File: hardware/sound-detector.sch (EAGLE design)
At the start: 36 parts, among them U1 LMV324

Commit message: Updating 3k3 resistor to Sparkle part.
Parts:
- R12: device SparkFun-Resistors:RESISTOR0603-RES -> SparkFun-Resistors:3.3KOHM1/10W1%(0603)
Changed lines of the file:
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@@
 <part name="GND7" library="SparkFun-Aesthetics" deviceset="GND" device=""/>
 <part name="R11" library="SparkFun-Resistors" deviceset="100KOHM1/10W1%(0603)" device="" value="100k"/>
-<part name="R12" library="SparkFun-Resistors" deviceset="RESISTOR" device="0603-RES" value="3k3"/>
+<part name="R12" library="SparkFun-Resistors" deviceset="3.3KOHM1/10W1%(0603)" device="" value="3k3"/>
 <part name="R13" library="SparkFun-Resistors" deviceset="1KOHM1/10W1%(0603)" device="" value="1K"/>
 <part name="R14" library="SparkFun-Resistors" deviceset="100KOHM1/10W1%(0603)" device="" value="100k"/>

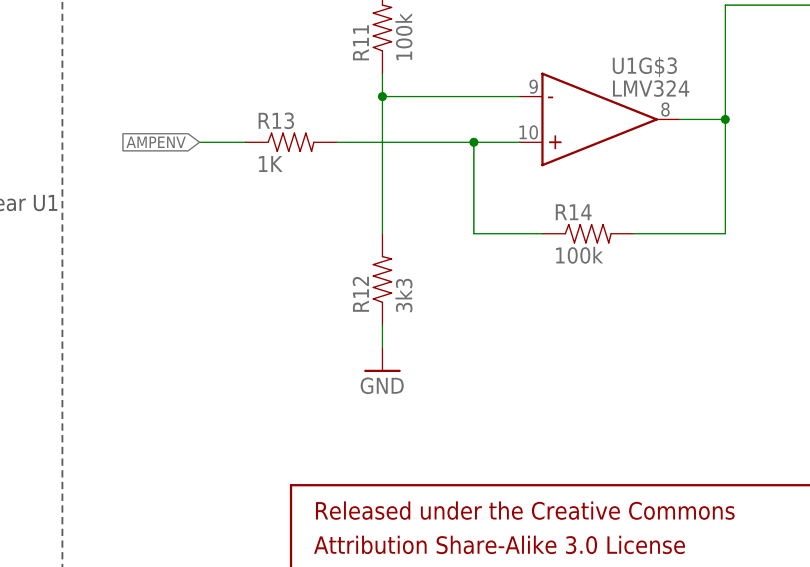
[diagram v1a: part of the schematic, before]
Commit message: Changing resistor value convention.
R12 changed from 3k3 to 3.3k.
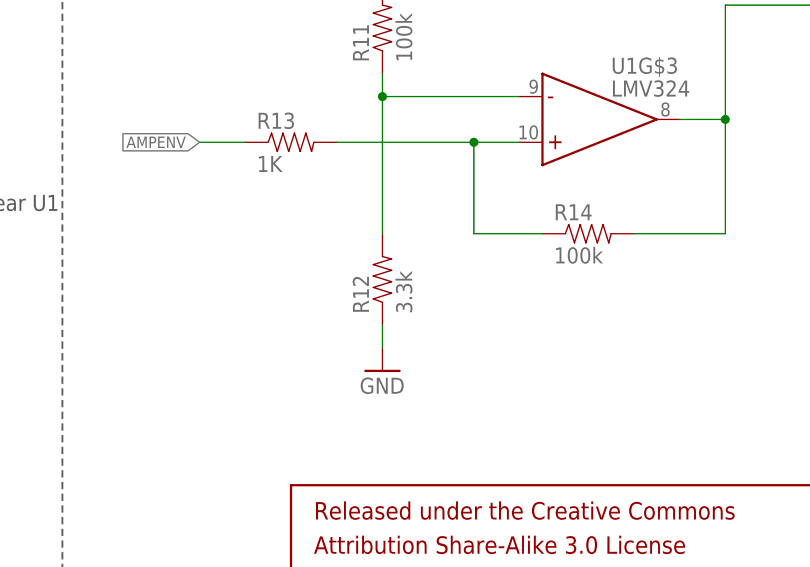
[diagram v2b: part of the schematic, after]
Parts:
- R12: value 3k3 -> 3.3k
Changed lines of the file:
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@@
 <part name="GND7" library="SparkFun-Aesthetics" deviceset="GND" device=""/>
 <part name="R11" library="SparkFun-Resistors" deviceset="100KOHM1/10W1%(0603)" device="" value="100k"/>
-<part name="R12" library="SparkFun-Resistors" deviceset="3.3KOHM1/10W1%(0603)" device="" value="3k3"/>
+<part name="R12" library="SparkFun-Resistors" deviceset="3.3KOHM1/10W1%(0603)" device="" value="3.3k"/>
 <part name="R13" library="SparkFun-Resistors" deviceset="1KOHM1/10W1%(0603)" device="" value="1K"/>
 <part name="R14" library="SparkFun-Resistors" deviceset="100KOHM1/10W1%(0603)" device="" value="100k"/>

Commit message: Changes based on green board review
-All text to vector
-fixed diode footprint to diodes.inc recommendations
--Added legend text for gain set resistors
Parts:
- R17: device SparkFun-Resistors:RESISTORPTH-1/4W-VERT -> SparkFun-Resistors:RESISTORPTH-1/4W-VERT-KIT
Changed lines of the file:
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@@
 <part name="R7" library="SparkFun-Resistors" deviceset="22KOHM1/10W1%(0603)" device="" value="22K"/>
 <part name="R18" library="SparkFun-Resistors" deviceset="100OHM1/10W1%(0603)" device="" value="100"/>
-<part name="R17" library="SparkFun-Resistors" deviceset="RESISTOR" device="PTH-1/4W-VERT" value="GAIN"/>
+<part name="R17" library="SparkFun-Resistors" deviceset="RESISTOR" device="PTH-1/4W-VERT-KIT" value="GAIN"/>
 <part name="R19" library="SparkFun-Resistors" deviceset="100OHM1/10W1%(0603)" device="" value="100"/>
 <part name="STANDOFF1" library="SparkFun-Electromechanical" deviceset="STAND-OFF" device=""/>

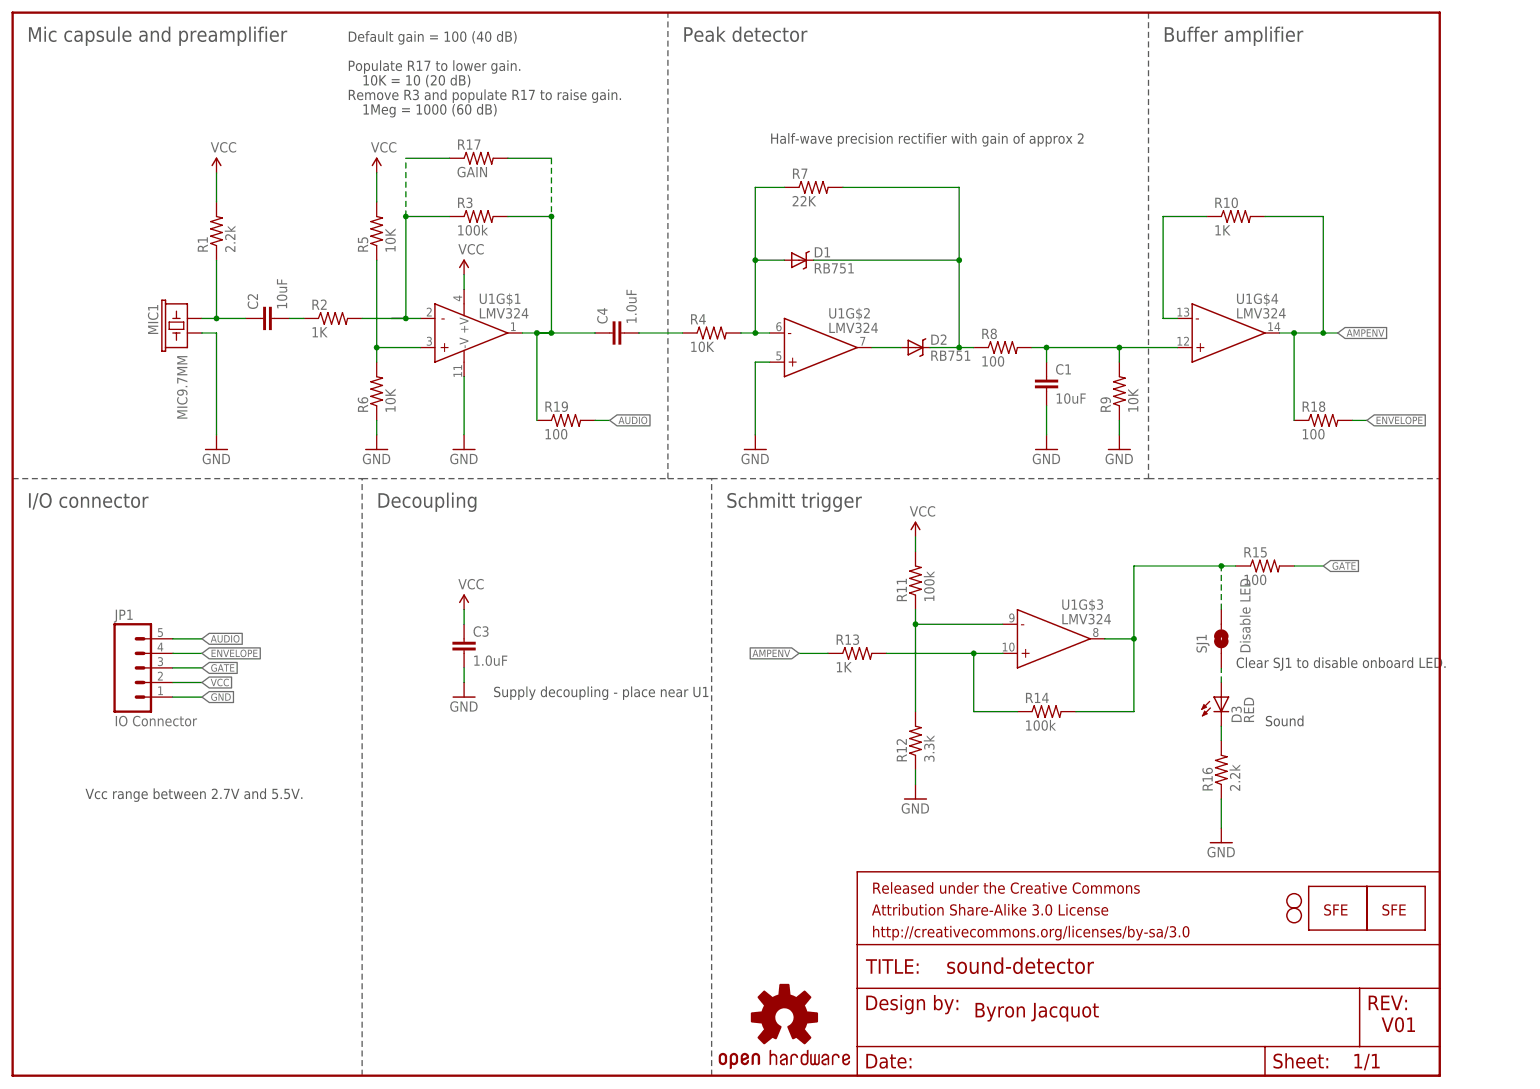
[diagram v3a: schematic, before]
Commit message: Ready for reds
Changed after group review:
-net width of schem
-Vector text
-IC naming
-Correct logos
-Minor electrical cleanup
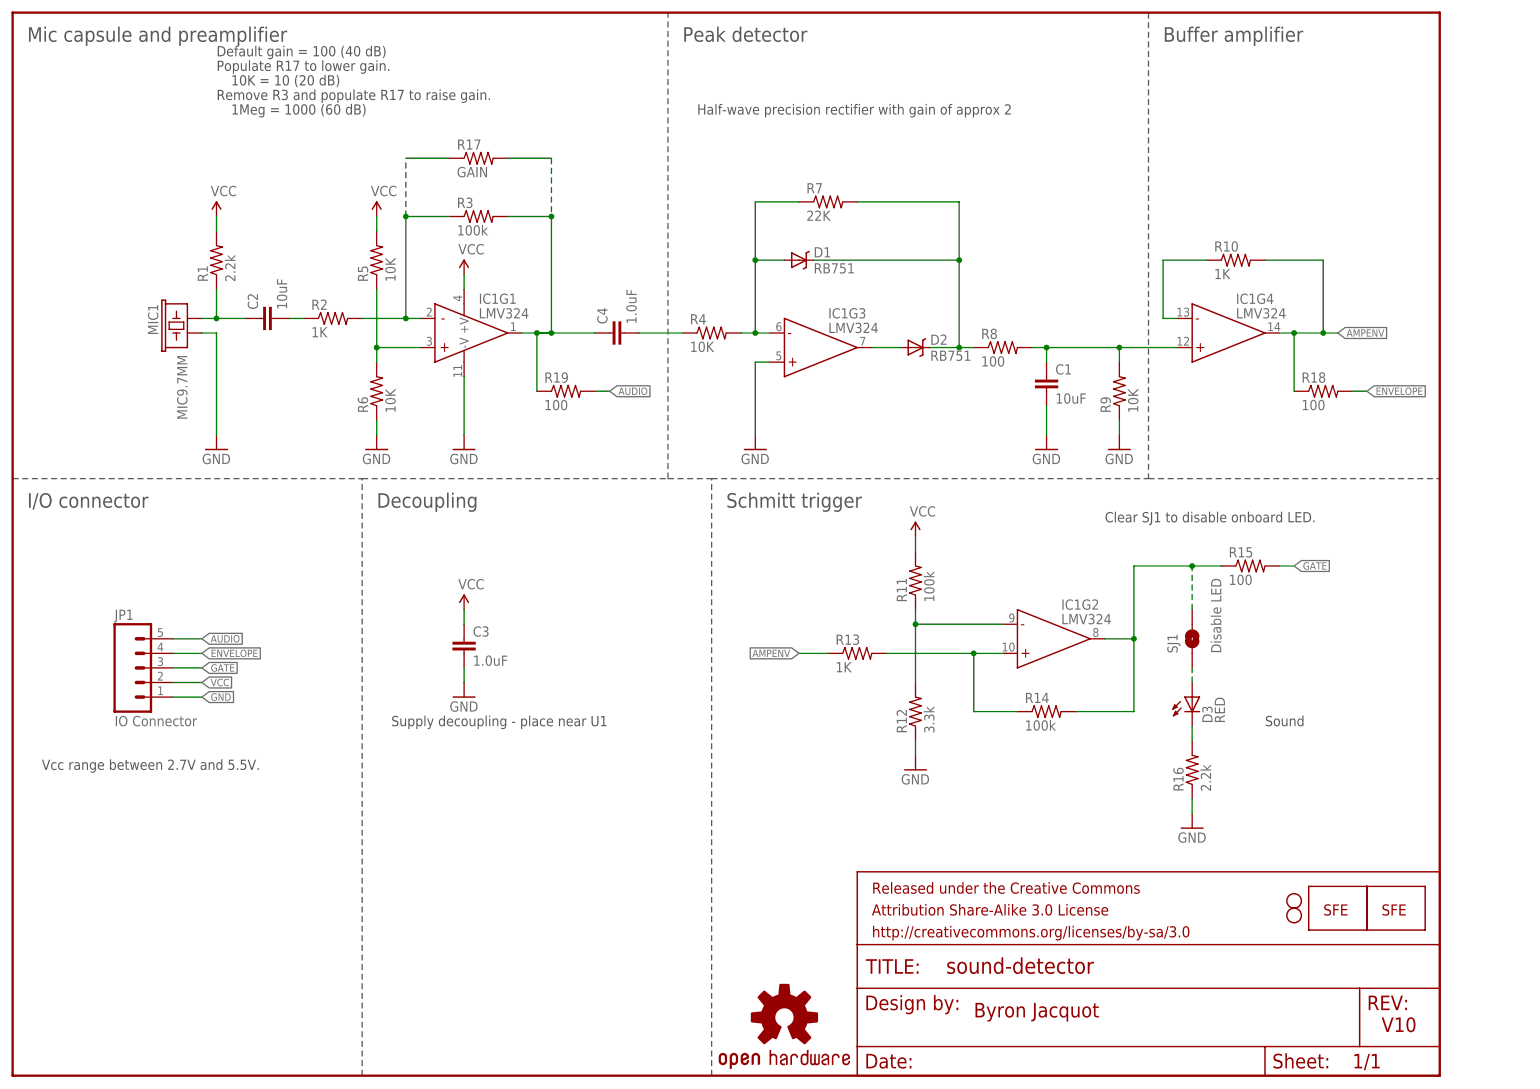
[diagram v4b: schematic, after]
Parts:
- removed U1: LMV324, SparkFun-AnalogIC:LMV324
- added IC1: LMV324, SparkFun-AnalogIC:LMV324
- LOGO2: value LOGO-SFENEW -> LOGO-SFENW2; device SparkFun-Aesthetics:LOGO-SFENEW -> SparkFun-Aesthetics:LOGO-SFENW2
- LOGO3: value LOGO-SFENW2 -> LOGO-SFESK; device SparkFun-Aesthetics:LOGO-SFENW2 -> SparkFun-Aesthetics:LOGO-SFESK
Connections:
- net AMPENV: now also IC1G4.OUT; no longer U1G$4.OUT
- net GND: now also IC1G1.-V, IC1G3.+IN; no longer U1G$1.-V, U1G$2.+IN
- net N$: now also IC1G1.OUT; no longer U1G$1.OUT
- net N$10: now also IC1G4.+IN; no longer U1G$4.+IN
- net N$11: now also IC1G4.-IN; no longer U1G$4.-IN
- net N$15: now also IC1G2.-IN; no longer U1G$3.-IN
- net N$16: now also IC1G2.+IN; no longer U1G$3.+IN
- net N$17: now also IC1G2.OUT; no longer U1G$3.OUT
- net N$2: now also IC1G1.+IN; no longer U1G$1.+IN
- net N$4: now also IC1G1.-IN; no longer U1G$1.-IN
- net N$7: now also IC1G3.-IN; no longer U1G$2.-IN
- net N$8: now also IC1G3.OUT; no longer U1G$2.OUT
- net VCC: now also IC1G1.+V; no longer U1G$1.+V
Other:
- note added: "V10"
- note removed: "V01"
- moved on the sheet: D3, R1, R10, R12, R15, R16, R18, R19, R5, R7, SJ1
